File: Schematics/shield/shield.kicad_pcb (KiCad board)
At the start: 2 copper layers, 80 x 66 mm, 57 parts, among them J1 RJ45, J2 RJ45, J3 J3, J4 J4, J5 J2, J6 J1, U1 P82B96, U2 P82B96, U3 OPA1622, U4 OPA1622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

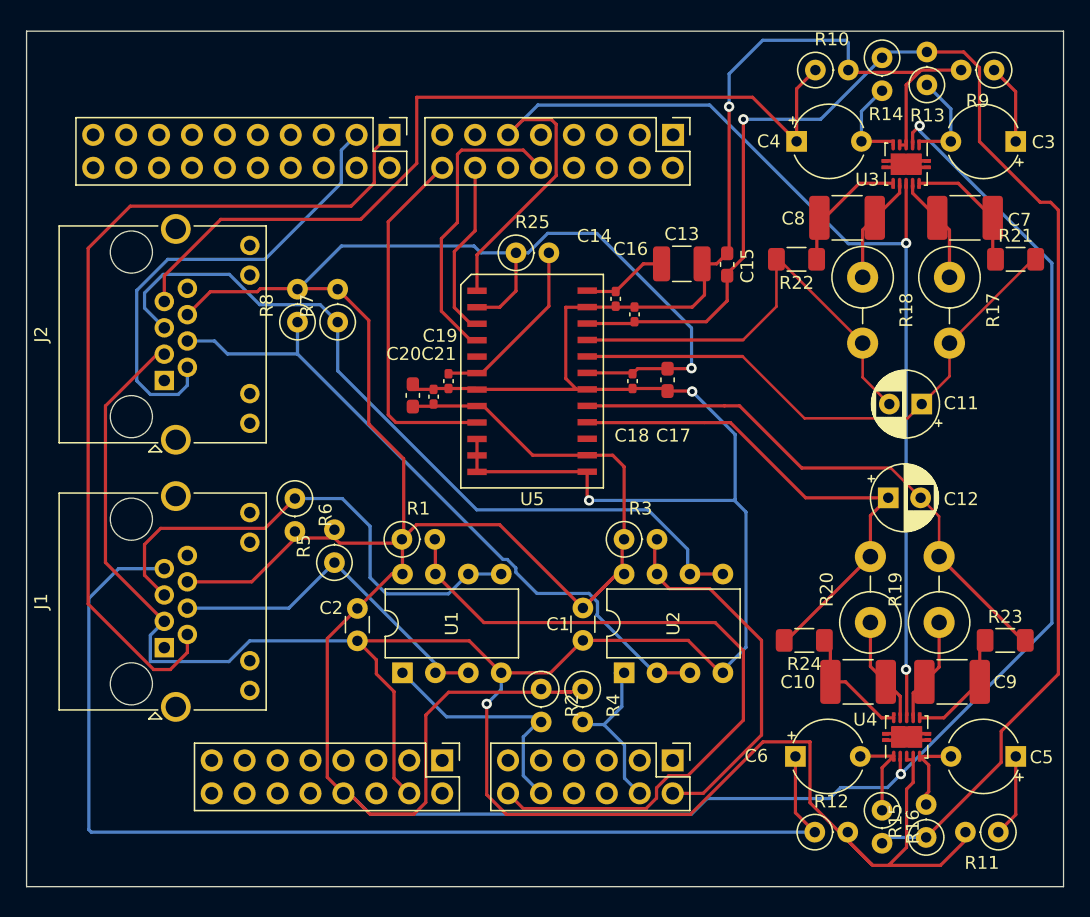
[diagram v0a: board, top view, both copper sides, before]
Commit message: Fixed Schematic. The FRDM K64F pin positions were one step too wide so narrowed and updated tracks. The pads for the I2S ADC IC were too narrow so wided to the maximum Spec. Updated Silkscreen to be useful
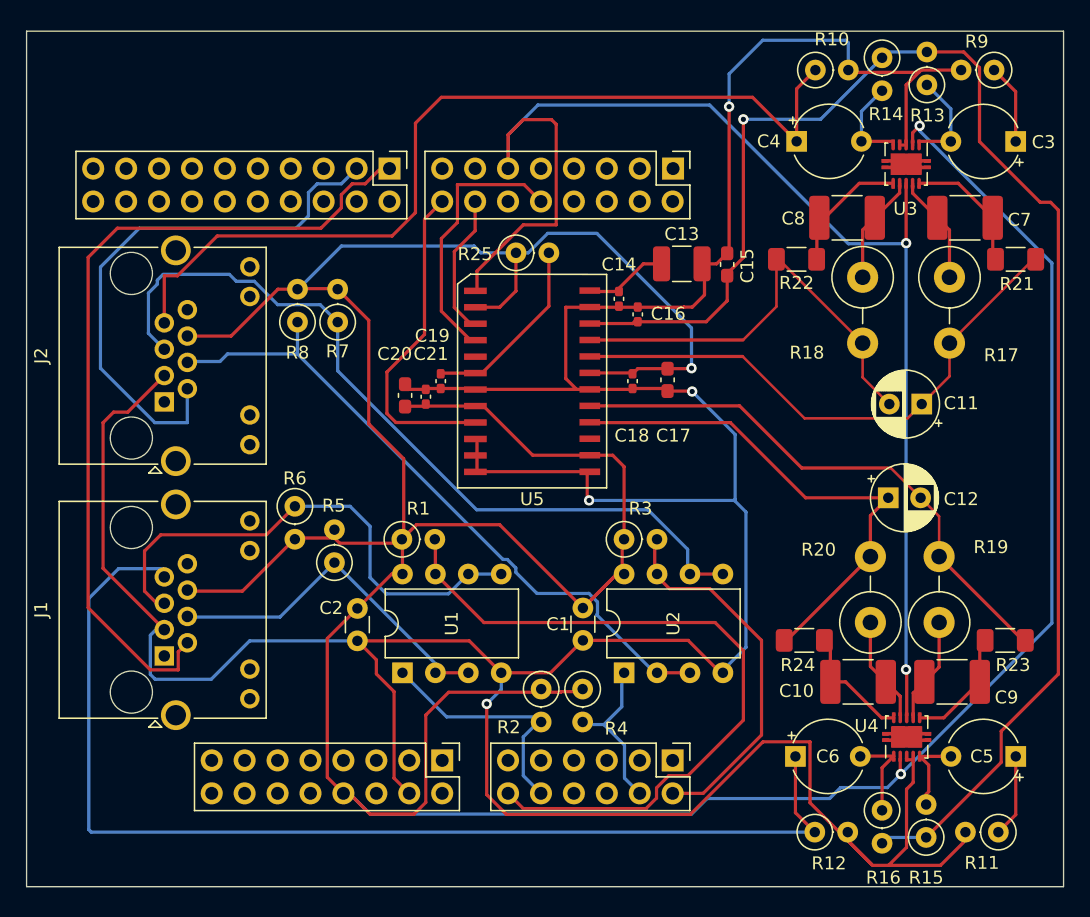
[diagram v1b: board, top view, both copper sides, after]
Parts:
- moved J5 2.60 mm to (100.0, 72.6)
- moved J6 2.60 mm to (121.8, 72.6)
- moved J2 1.65 mm to (82.6, 90.6)
- moved J1 0.64 mm to (82.6, 110.2)
- moved C21 0.60 mm to (102.8, 90.2)
- moved C19 0.60 mm to (104.0, 89.0)
- moved C20 0.60 mm to (101.2, 90.1)
- moved R6 0.60 mm to (92.7, 98.7)
- moved C14 0.25 mm to (117.7, 82.7)
- moved C16 0.25 mm to (119.2, 83.8)
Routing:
- net D5: track 96.8 -> 103.5 mm
- net D9: track 36.4 -> 43.1 mm
- net +5V: track 316.6 -> 313.2 mm
- net D8: track 67.5 -> 64.3 mm
- net D6B: track 13.7 -> 10.6 mm
- net D4B: track 23.4 -> 20.4 mm
- net J2_Audio: track 67.2 -> 69.9 mm
- net D7B: track 27.9 -> 25.4 mm
- net VQ: track 117.7 -> 115.7 mm
- net SCL2: track 61.2 -> 62.6 mm
- net Net-(C10-Pad2): track 9.43 -> 8.77 mm
- net GND: track 295.4 -> 294.8 mm
- net Net-(C9-Pad2): track 9.16 -> 8.57 mm
- net A4: track 13.2 -> 12.7 mm
